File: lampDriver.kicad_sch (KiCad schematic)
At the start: 0 parts

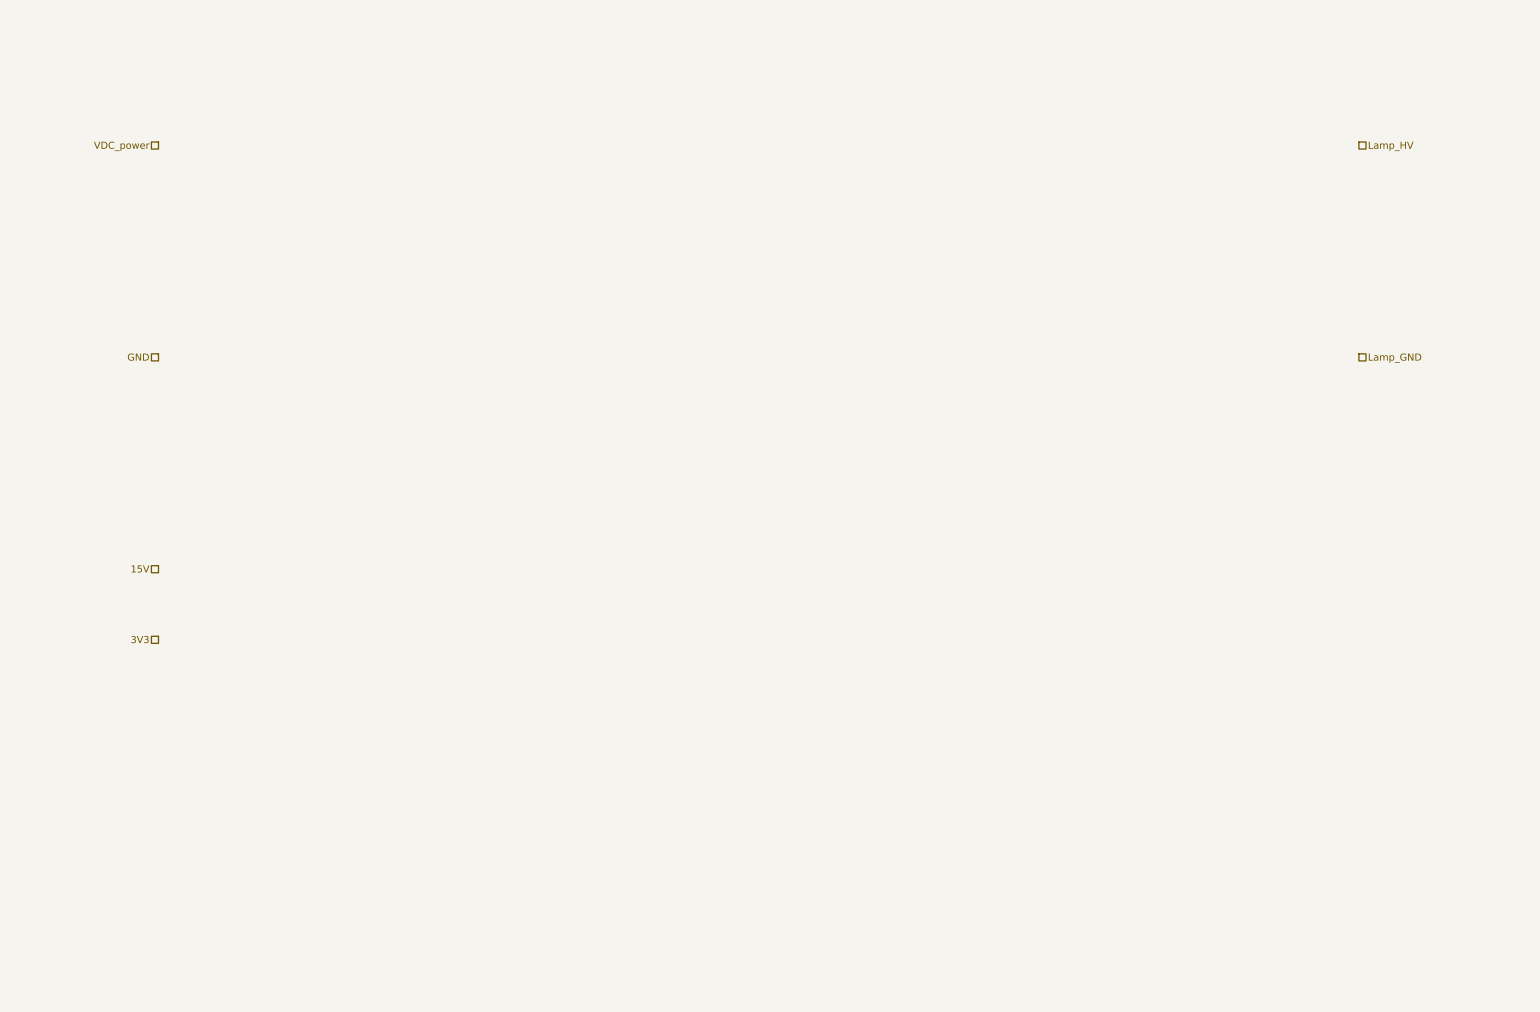
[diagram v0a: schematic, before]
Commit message: update of schematic
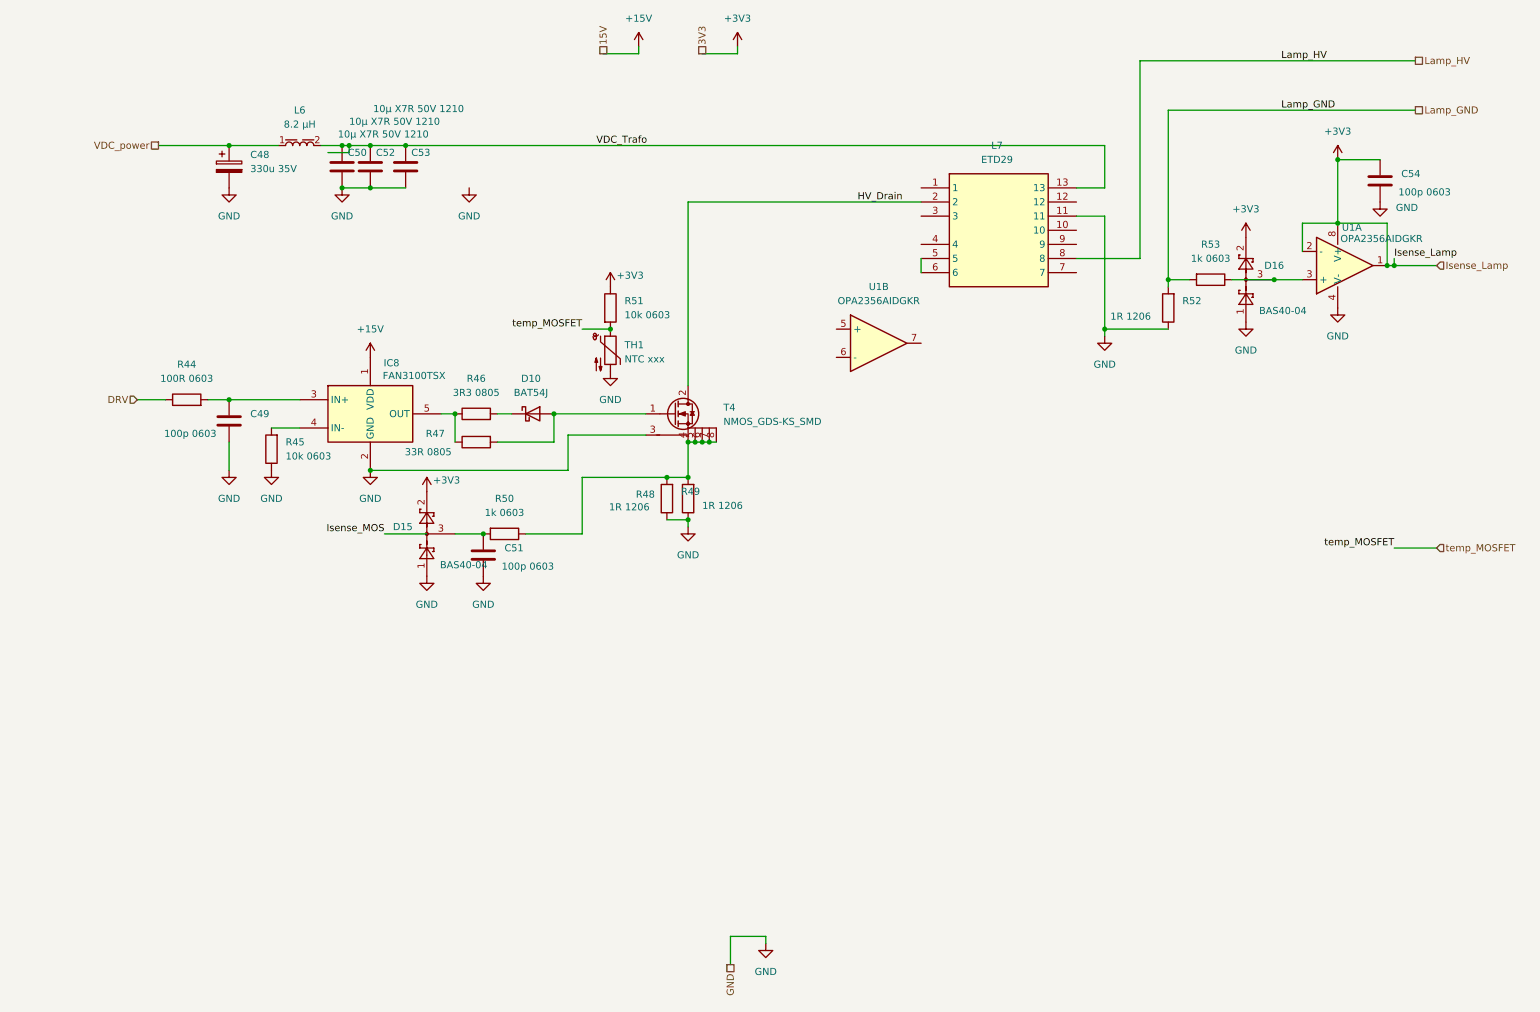
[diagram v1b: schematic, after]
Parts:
- added C48: 330u 35V, Capacitor_THT:CP_Radial_D13.0mm_P5.00mm, symbol Device:C_Polarized
- added C49, C51, C54: 100p 0603, Capacitor_SMD:C_0603_1608Metric, symbol Device:C
- added C50, C52, C53: 10µ X7R 50V 1210, Capacitor_SMD:C_1210_3225Metric, symbol Device:C
- added D10: BAT54J, Diode_SMD:D_SOD-323F, symbol Diode:BAT54J
- added D15, D16: BAS40-04, Package_TO_SOT_SMD:SOT-23, symbol Diode:BAS40-04
- added IC8: FAN3100TSX, SOT95P280X145-5N, symbol Hansmann:FAN3100TSX
- added L6: 1812_744045008, Inductor_SMD_Wurth:L_Wurth_WE-LQ-1812, symbol Inductor_Wurth_WE-LQ:1812_744045008
- added L7: ETD29, B66359B1013T001, symbol Hansmann:ETD29
- added R44: 100R 0603, Resistor_SMD:R_0603_1608Metric, symbol Device:R
- added R45, R51: 10k 0603, Resistor_SMD:R_0603_1608Metric, symbol Device:R
- added R46: 3R3 0805, Resistor_SMD:R_0805_2012Metric, symbol Device:R
- added R47: 33R 0805, Resistor_SMD:R_0805_2012Metric, symbol Device:R
- added R48, R49, R52: 1R 1206, Resistor_SMD:R_1206_3216Metric, symbol Device:R
- added R50, R53: 1k 0603, Resistor_SMD:R_0603_1608Metric, symbol Device:R
- added T4: NMOS_GDS-KS_SMD, Hansmann:TO-263-7_TabPin2, symbol Hansmann:NMOS_GDS-KS_SMD
- added TH1: NTC xxx, Resistor_SMD:R_0805_2012Metric, symbol Device:Thermistor_NTC
- added U1: OPA2356AIDGKR, Package_SO:VSSOP-8_3x3mm_P0.65mm, symbol Device:Opamp_Dual
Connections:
- net GND: now also C48.2, C49.2, C50.2, C51.2, C52.2, C53.2, C54.2, D15.1, D16.1, IC8.2 (GND), L7.11, R45.1, R48.1, R49.1, R52.1, T4.3 (KS), TH1.2, U1.4 (V-)
- net Lamp_GND: now also R52.2, R53.2
- net Lamp_HV: now also L7.8
- net VDC_power: now also C48.1, L6.1
- new net: R48.2, R49.2, R50.1, T4.4 (S), T4.5 (S), T4.6 (S), T4.7 (S), T4.8 (S)
- new net: C49.1, IC8.3 (IN+), R44.2
- new net: D16.3, R53.1, U1.3 (+)
- new net: IC8.4 (IN-), R45.2
- new net: L7.5, L7.6
- new net: IC8.5 (OUT), R46.1, R47.1
- new net: D10.2 (A), R47.2, T4.1 (G)
- new net: C51.1, D15.3, R50.2
- new net: D10.1 (K), R46.2
- new net +15V: IC8.1 (VDD)
- new net +3V3: C54.1, D15.2, D16.2, R51.1, U1.1, U1.2 (-), U1.8 (V+)
- new net DRV: R44.1
- new net HV_Drain: L7.2, T4.2 (D)
- new net VDC_Trafo: C50.1, C52.1, C53.1, L6.2, L7.13
- new net temp_MOSFET: R51.2, TH1.1

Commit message: schematic done, not placed
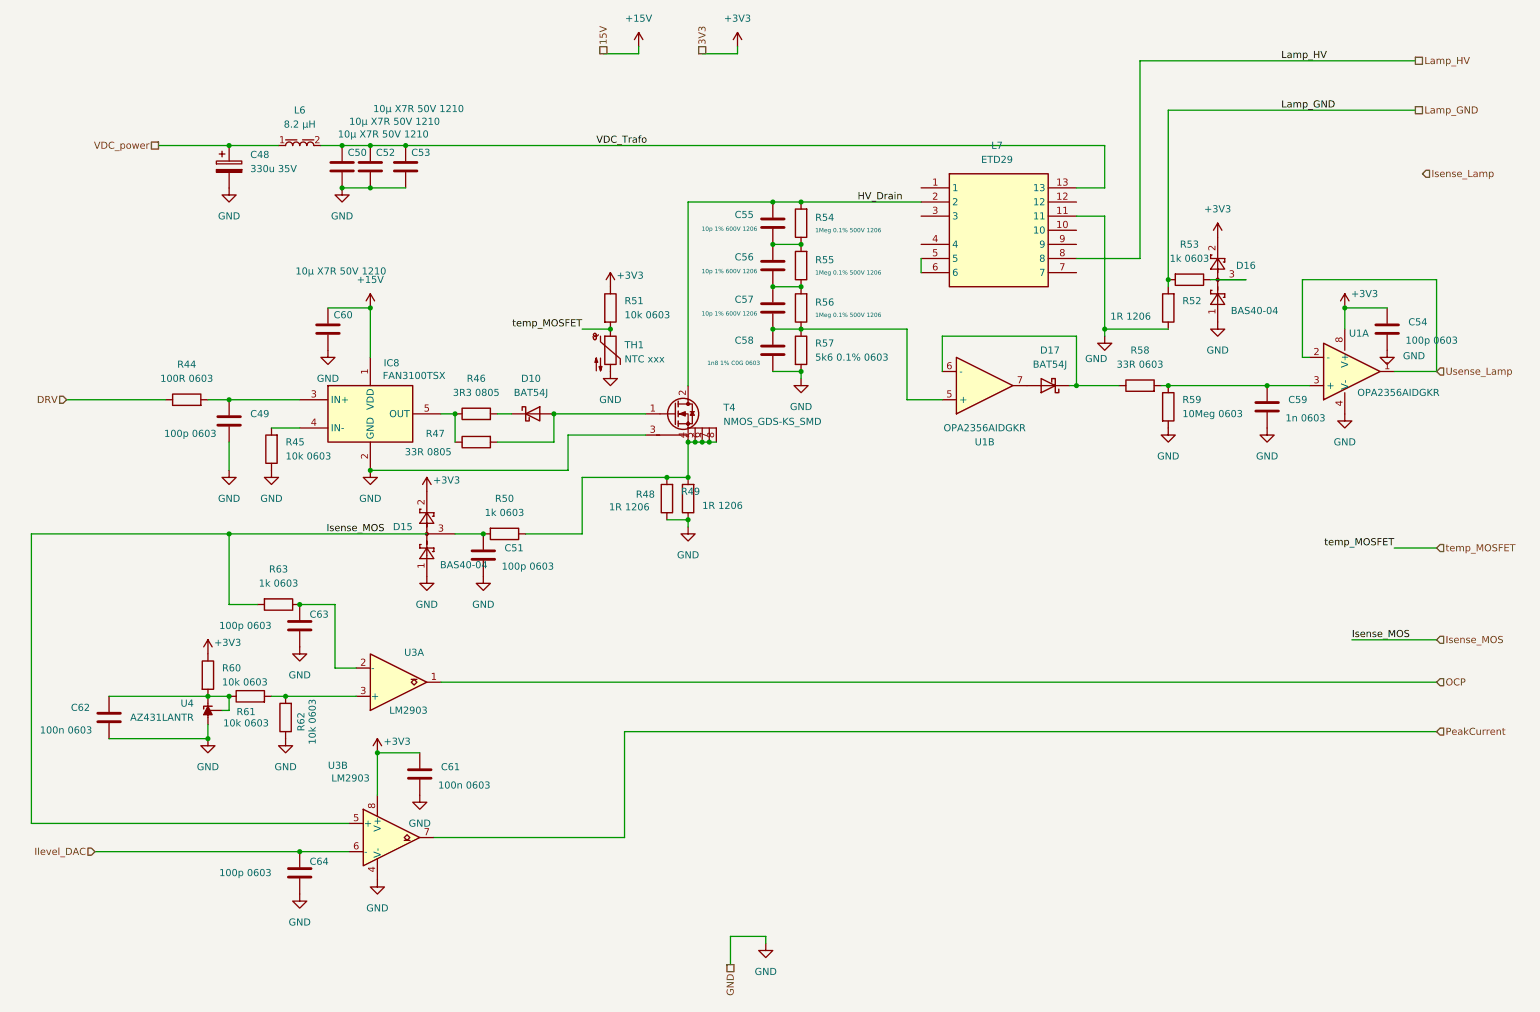
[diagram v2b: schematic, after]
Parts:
- added C55, C56, C57: 10p 1% 600V 1206, Capacitor_SMD:C_1206_3216Metric, symbol Device:C
- added C58: 1n8 1% C0G 0603, Capacitor_SMD:C_0603_1608Metric, symbol Device:C
- added C59: 1n 0603, Capacitor_SMD:C_0603_1608Metric, symbol Device:C
- added C60: 10µ X7R 50V 1210, Capacitor_SMD:C_1210_3225Metric, symbol Device:C
- added C61, C62: 100n 0603, Capacitor_SMD:C_0603_1608Metric, symbol Device:C
- added C63, C64: 100p 0603, Capacitor_SMD:C_0603_1608Metric, symbol Device:C
- added D17: BAT54J, Diode_SMD:D_SOD-323F, symbol Diode:BAT54J
- added R54, R55, R56: 1Meg 0.1% 500V 1206, Resistor_SMD:R_1206_3216Metric, symbol Device:R
- added R57: 5k6 0.1% 0603, Resistor_SMD:R_0603_1608Metric, symbol Device:R
- added R58: 33R 0603, Resistor_SMD:R_0603_1608Metric, symbol Device:R
- added R59: 10Meg 0603, Resistor_SMD:R_0603_1608Metric, symbol Device:R
- added R60, R61, R62: 10k 0603, Resistor_SMD:R_0603_1608Metric, symbol Device:R
- added R63: 1k 0603, Resistor_SMD:R_0603_1608Metric, symbol Device:R
- added U3: LM2903, Package_SO:TSSOP-8_4.4x3mm_P0.65mm, symbol Comparator:LM2903
- added U4: AZ431LANTR, Package_TO_SOT_SMD:SOT-23, symbol Reference_Voltage:TL432DBZ
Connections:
- net +15V: now also C60.1
- net +3V3: now also C61.1, R60.1, U3.8 (V+); no longer U1.1, U1.2 (-)
- net GND: now also C58.2, C59.2, C60.2, C61.2, C62.2, C63.2, C64.2, R57.2, R59.2, R62.1, U3.4 (V-), U4.3 (A)
- net HV_Drain: now also C55.1, R54.2
- net Isense_MOS: now also R63.2, U3.5 (+)
- net at D16.3, R53.1: no longer U1.3 (+)
- net at U1.5 (+): now also C57.2, C58.1, R56.1, R57.1
- net at U1.6 (-): now also D17.1 (K), R58.1
- net at U1.7: now also D17.2 (A)
- new net: C59.1, R58.2, R59.1, U1.3 (+)
- new net: C55.2, C56.1, R54.1, R55.2
- new net: C62.1, R60.2, R61.1, U4.1 (REF), U4.2 (K)
- new net: R61.2, R62.2, U3.3 (+)
- new net: C56.2, C57.1, R55.1, R56.2
- new net: C63.1, R63.1, U3.2 (-)
- new net Ilevel_DAC: C64.1, U3.6 (-)
- new net OCP: U3.1
- new net PeakCurrent: U3.7
- new net Usense_Lamp: U1.1, U1.2 (-)
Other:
- moved on the sheet: C54, D16, R53, U1A, U1B

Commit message: restore to 9.0
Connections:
- net at IC8.5 (OUT), R47.1: now also D10.1 (K); no longer R46.1
- net at R47.2, T4.1 (G): now also R46.2; no longer D10.2 (A)
- new net: D10.2 (A), R46.1
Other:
- moved on the sheet: D10, R46

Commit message: 250415_endOfDay
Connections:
- net Isense_MOS: now also C51.1, D15.3, R50.2
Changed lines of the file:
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@@
+	)
+	(junction
+		(at 175.26 60.96)
+		(diameter 0)
+		(color 0 0 0 0)
 	)
 	(junction
@@
 	)
 	(junction
+		(at 91.44 107.95)
+		(diameter 0)
+		(color 0 0 0 0)
+	)
+	(junction
 		(at 76.2 67.31)
 		(diameter 0)
@@
 	(wire
 		(pts
+			(xy 175.26 60.96) (xy 175.26 63.5)
+		)
+		(stroke
+			(width 0)
+			(type default)
+		)
+	)
+	(wire
+		(pts
 			(xy 208.28 50.8) (xy 208.28 71.12)
 		)
@@
 	(wire
 		(pts
-			(xy 50.8 107.95) (xy 86.36 107.95)
+			(xy 50.8 107.95) (xy 91.44 107.95)
 		)
 		(stroke
@@
 			(fill
 				(type none)
+			)
+		)
+	)
+	(netclass_flag ""
+		(length 2.54)
+		(shape round)
+		(at 153.67 63.5 270)
+		(effects
+			(font
+				(size 1.27 1.27)
+			)
+			(justify right bottom)
+		)
+		(property "Net Class" "HV_Drain_div2"
+			(at 157.734 63.246 0)
+			(effects
+				(font
+					(size 1.27 1.27)
+				)
+				(justify left)
+			)
+		)
+		(property "Component Class" ""
+			(at -49.53 8.89 0)
+			(effects
+				(font
+					(size 1.27 1.27)
+					(italic yes)
+				)
+			)
+		)
+	)
+	(netclass_flag ""
+		(length 2.54)
+		(shape round)
+		(at 153.67 55.88 270)
+		(effects
+			(font
+				(size 1.27 1.27)
+			)
+			(justify right bottom)
+		)
+		(property "Net Class" "HV_Drain_div"
+			(at 157.226 55.88 0)
+			(effects
+				(font
+					(size 1.27 1.27)
+				)
+				(justify left)
+			)
+		)
+		(property "Component Class" ""
+			(at -48.26 1.27 0)
+			(effects
+				(font
+					(size 1.27 1.27)
+					(italic yes)
+				)
+			)
+		)
+	)
+	(netclass_flag ""
+		(length 2.54)
+		(shape round)
+		(at 175.26 63.5 180)
+		(fields_autoplaced yes)
+		(effects
+			(font
+				(size 1.27 1.27)
+			)
+			(justify right bottom)
+		)
+		(property "Net Class" "HV_Lamp/2"
+			(at 175.9585 66.04 0)
+			(effects
+				(font
+					(size 1.27 1.27)
+				)
+				(justify left)
+			)
+		)
+		(property "Component Class" ""
+			(at -44.45 31.75 0)
+			(effects
+				(font
+					(size 1.27 1.27)
+					(italic yes)
+				)
 			)
 		)
@@
 			(effects
 				(font
+					(size 1.27 1.27)
+					(italic yes)
+				)
+			)
+		)
+	)
+	(netclass_flag ""
+		(length 2.54)
+		(shape round)
+		(at 214.63 22.86 0)
+		(fields_autoplaced yes)
+		(effects
+			(font
+				(size 1.27 1.27)
+			)
+			(justify left bottom)
+		)
+		(property "Net Class" "HV_Lamp"
+			(at 215.3285 20.32 0)
+			(effects
+				(font
+					(size 1.27 1.27)
+				)
+				(justify left)
+			)
+		)
+		(property "Component Class" ""
+			(at -73.66 -6.35 0)
+			(effects
+				(font
